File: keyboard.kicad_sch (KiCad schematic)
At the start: 10 parts

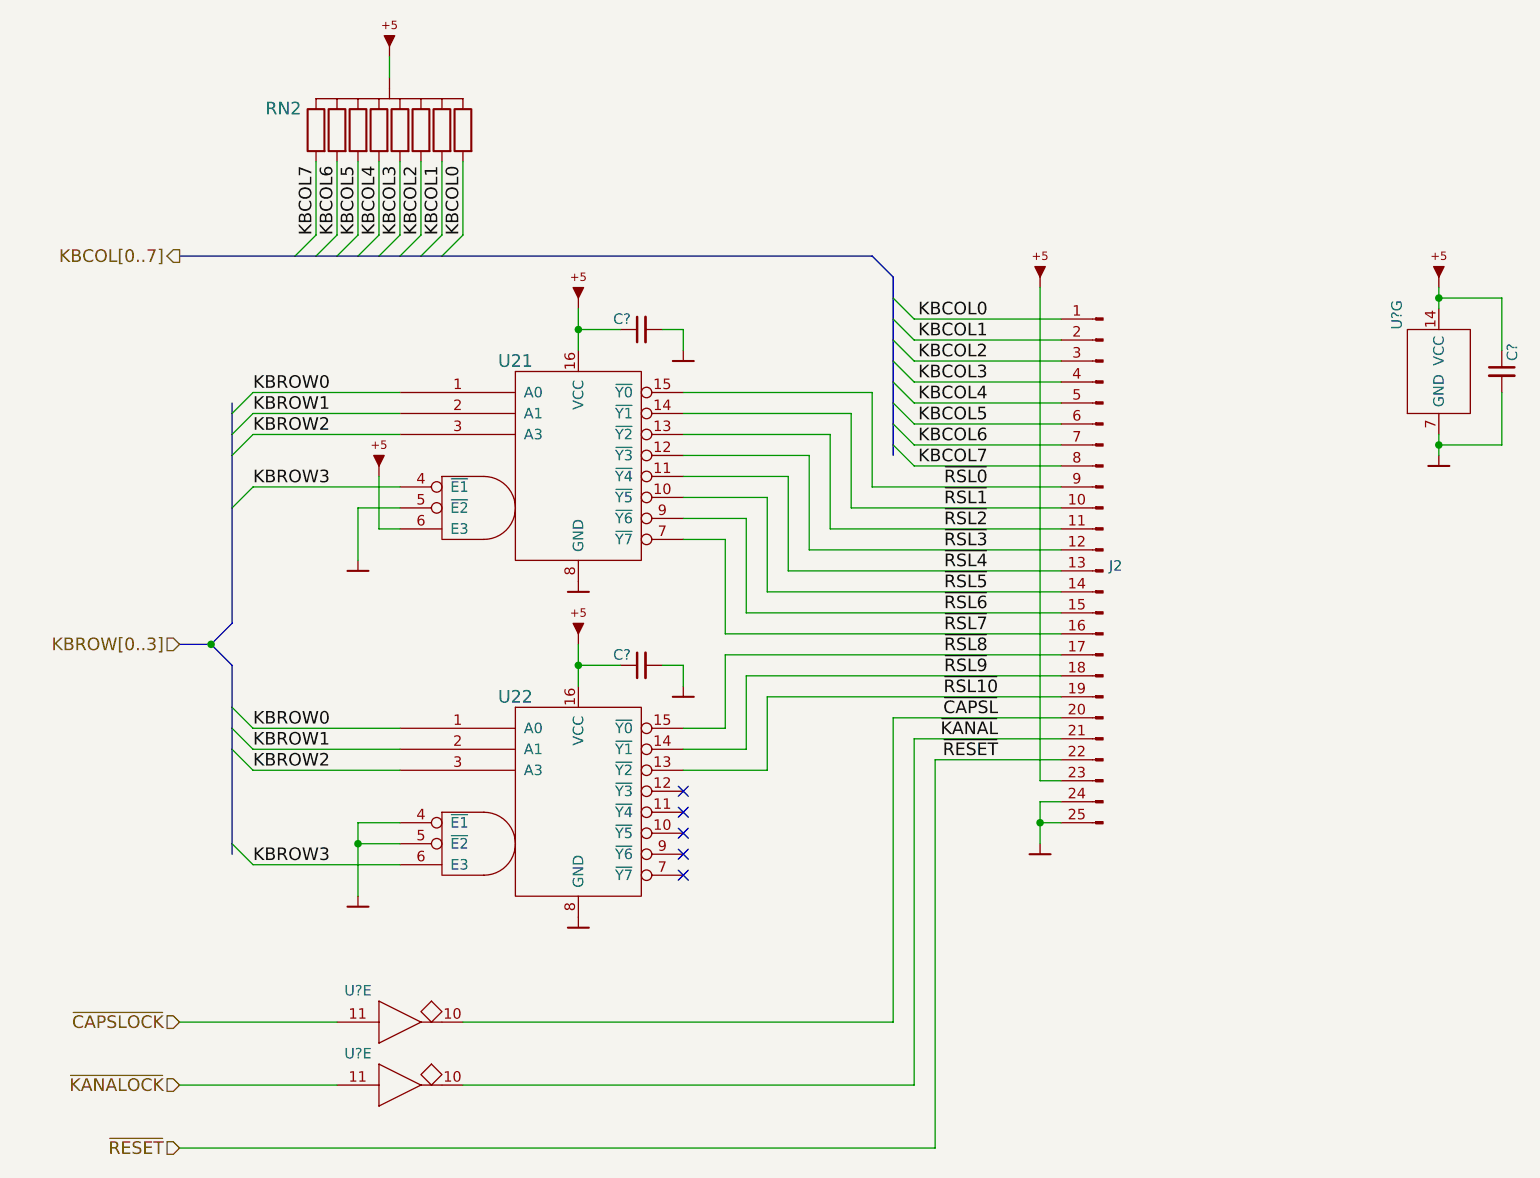
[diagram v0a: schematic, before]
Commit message: Implement power transform circuit
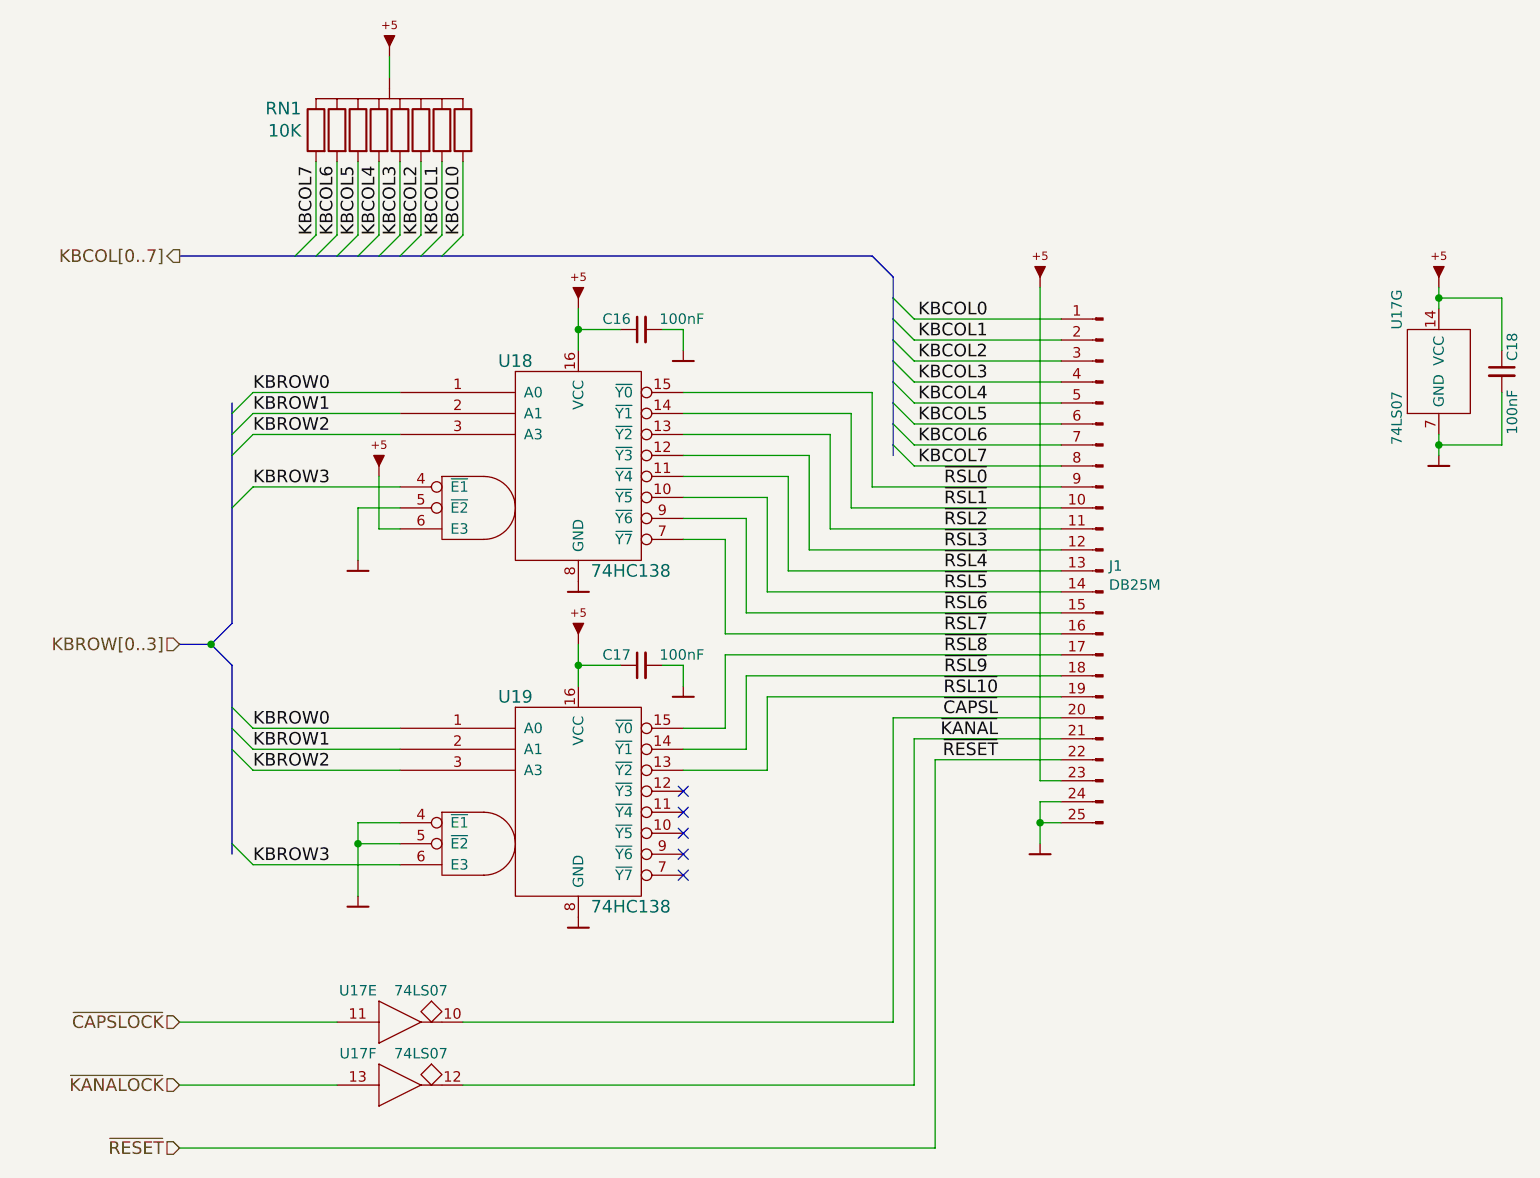
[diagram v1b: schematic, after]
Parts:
- C16, C17, C18: renamed from C?; value (none) -> 100nF; footprint (none) -> artemisa:Disc_capacitor
- J1: renamed from J2; value (none) -> DB25M; footprint (none) -> artemisa:DB25M
- RN1: renamed from RN2; value (none) -> 10K; footprint (none) -> artemisa:RN8
- U17: renamed from U?; value (none) -> 74LS07; footprint (none) -> artemisa:DIP-14_300
- U18: renamed from U21; value (none) -> 74HC138; footprint (none) -> artemisa:DIP-16_300
- U19: renamed from U22; value (none) -> 74HC138; footprint (none) -> artemisa:DIP-16_300
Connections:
- net ~{KANALOCK}: now also U17.13; no longer U17.11
- net ~{KANAL}: now also U17.12; no longer U17.10
- net VCC: now reaches RN1.1
- net VCC: now also C16.1, C17.1, C18.1, J1.23 (Pin_23), U17.14 (VCC), U18.16 (VCC), U18.6 (E3), U19.16 (VCC)
